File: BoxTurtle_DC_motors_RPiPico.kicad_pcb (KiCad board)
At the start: 4 copper layers, 99.1 x 73.7 mm, 81 parts, among them J1 Power input, J10 DC motor 1, J11 DC motor 2, J12 DC motor 3, J13 DC motor 4, J14 Screw_Terminal_01x02, J15 CAN, J2 Power input, J3 Power output, J4 Power output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

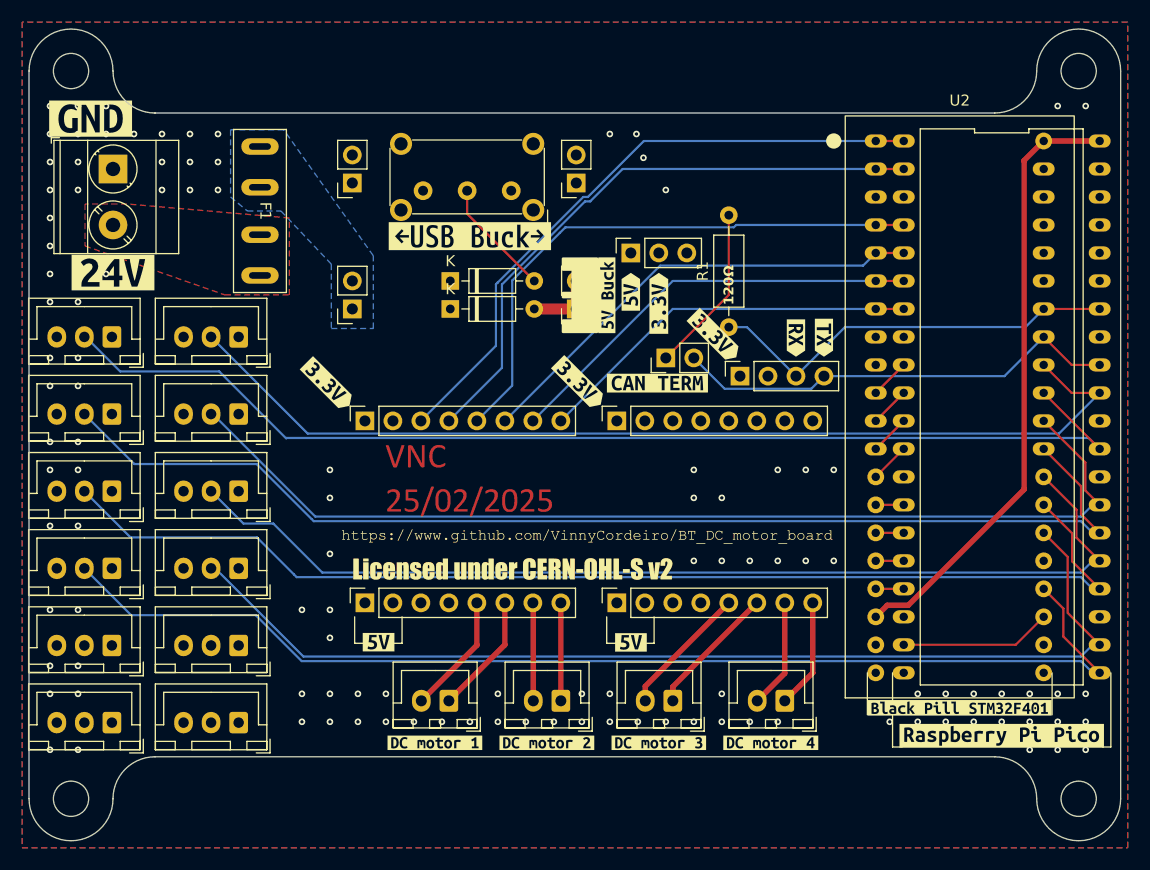
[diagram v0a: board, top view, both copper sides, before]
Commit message: Revision 2.6
Updated footprints again now that I have them on hand to accurately make measures, changed selection switch for a model that is smaller and carry more current.
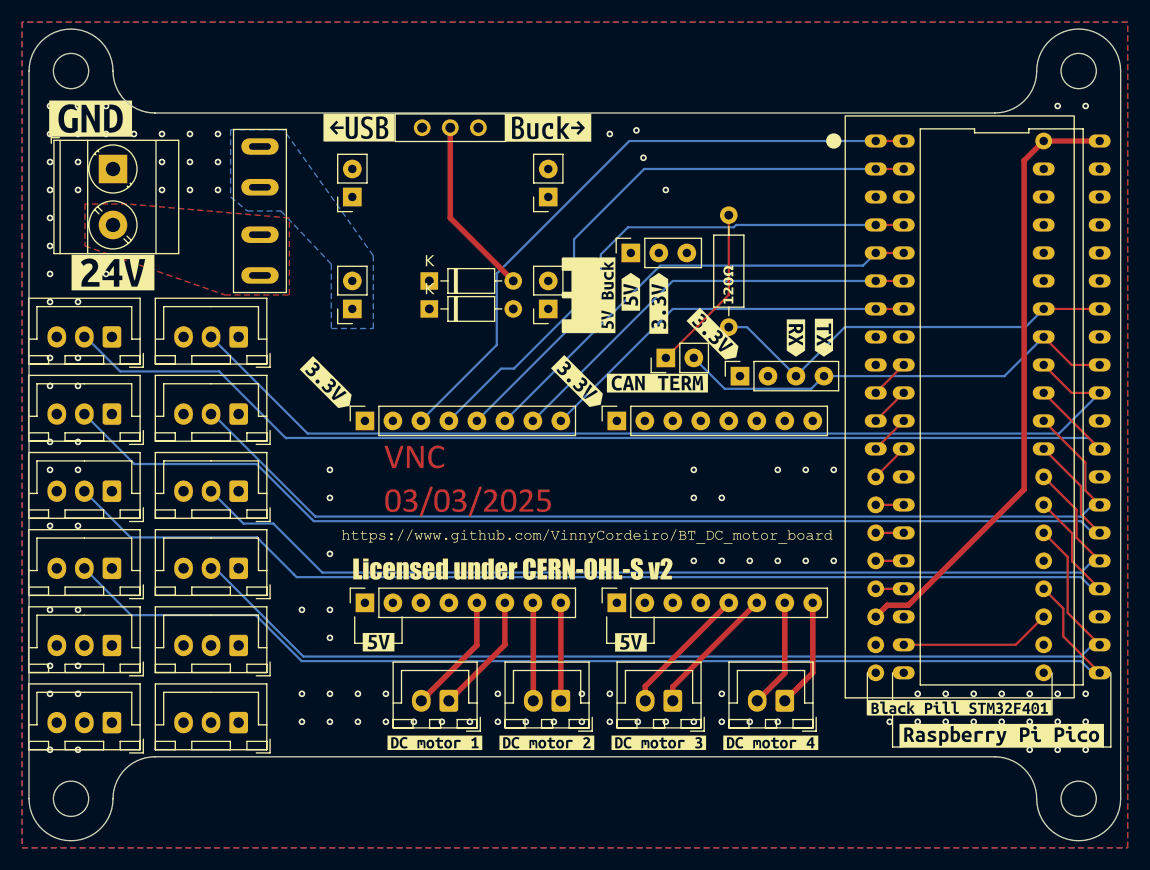
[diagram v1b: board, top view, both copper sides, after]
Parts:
- removed kibuzzard-67A00B69: G***, kibuzzard-67A00B69
- removed kibuzzard-67A00BD4: G***, kibuzzard-67A00BD4
- added kibuzzard-67C5FAD7: G***, kibuzzard-67C5FAD7, F.Cu at (123.9, 44.5)
- added kibuzzard-67C5FB16: G***, kibuzzard-67C5FB16, B.Cu at (123.9, 44.5)
- added kibuzzard-67C5FB88: G***, kibuzzard-67C5FB88, F.Cu at (141.1, 44.5)
- added kibuzzard-67C5FBBE: G***, kibuzzard-67C5FBBE, B.Cu at (141.1, 44.5)
- SW13: value EG1224 -> K3-1204D; footprint Button_Switch_THT:SW_E-Switch_EG1224_SPDT_Angled -> K3-1204D:K3-1204D
- moved SW13 7.95 mm to (132.2, 44.5)
- moved J4 2.84 mm to (141.1, 50.8)
- moved J3 2.54 mm to (141.1, 61.0)
- moved D1 1.91 mm to (130.3, 58.4)
- moved D2 1.91 mm to (130.3, 61.0)
- moved J2 1.27 mm to (123.3, 50.8)
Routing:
- net +5VBUCK: track 6.35 -> 0.00 mm
- net Net-(D1-A): track 10.7 -> 16.3 mm
- net DC2_1: track 51.7 -> 48.4 mm
- net VBUS: track 116.6 -> 118.6 mm
- net DC1_1: track 55.2 -> 54.4 mm
- net SLP_1: track 57.6 -> 58.1 mm
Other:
- board text added: "BoxTurtle DC motors standalone board Rev 2.6"
- board text removed: "BoxTurtle DC motors standalone board Rev 2.5"

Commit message: Revision 2.6.1
Just silkscreen changes
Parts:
- removed kibuzzard-67A0C0D2 (x4): G***, kibuzzard-67A0C0D2
- removed kibuzzard-67A0C14A: G***, kibuzzard-67A0C14A
- removed kibuzzard-67A0C703: G***, kibuzzard-67A0C703
- removed kibuzzard-67A0CDC3: G***, kibuzzard-67A0CDC3
- removed kibuzzard-67A0CDFB: G***, kibuzzard-67A0CDFB
- added kibuzzard-67C627D9: G***, kibuzzard-67C627D9, F.Cu at (125.7, 90.4)
- added kibuzzard-67C627E2: G***, kibuzzard-67C627E2, F.Cu at (148.6, 90.4)
- added kibuzzard-67C627EC: G***, kibuzzard-67C627EC, F.Cu at (121.6, 68.2)
- added kibuzzard-67C627F5: G***, kibuzzard-67C627F5, F.Cu at (144.4, 68.2)
- added kibuzzard-67C6285C: G***, kibuzzard-67C6285C, B.Cu at (121.6, 68.2)
- added kibuzzard-67C6289C: G***, kibuzzard-67C6289C, B.Cu at (144.4, 68.2)
- added kibuzzard-67C628B6: G***, kibuzzard-67C628B6, B.Cu at (148.5, 90.4)
- added kibuzzard-67C628BD: G***, kibuzzard-67C628BD, B.Cu at (125.7, 90.4)
- moved kibuzzard-679EE822 2.45 mm to (156.2, 63.4), turned to -45 degrees
- moved kibuzzard-67A0CA07 1.02 mm to (145.4, 59.7)
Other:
- board text added: "BoxTurtle DC motors standalone board Rev 2.6.1"
- board text removed: "BoxTurtle DC motors standalone board Rev 2.6"
